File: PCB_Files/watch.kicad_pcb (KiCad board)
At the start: 4 copper layers, 40 x 40 mm, 118 parts, among them J1 Conn_01x13_MountingPin, J3 Conn_01x02_Pin, P1 USB_C_Plug_USB2.0, Q1 BC847, Q2 BC847, Q3 FS8205A, Q4 BSS138, Q5 BSS138, Q8 BC847, SW1 SW_Push, SW2 SW_Push, U1 APS6404L-3SQRx-ZR, U10 LSM6DS3, U11 MAX-M10S, U12 MCP1700x-120xxMB, U13 DRV2605LDGS, U2 ESP32-PICO-D4, U3 CP2102N-Axx-xQFN28, U4 TPS7A0533PDBV, U5 MCP73831-2-OT, U6 AP9101CK6, U7 MAX30105EFD_T, U8 W25Q128JVS, U9 BMP388, Y1 SG-3030CM

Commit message: Added new ZIF connector footprint and made changes in schematics
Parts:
- moved AE1 89.0 mm to (131.4, 82.7)
- moved TP2 79.3 mm to (143.6, 92.6)
- moved TP1 76.5 mm to (145.6, 92.6)
- moved TP3 71.2 mm to (153.8, 93.8)
- moved TP5 71.0 mm to (156.1, 96.9)
- moved TP4 71.0 mm to (154.1, 96.6)
- moved TP6 69.6 mm to (158.5, 96.9)
- moved C31 3.91 mm to (160.7, 99.6), turned to -90 degrees
- moved C19 3.43 mm to (157.2, 90.2)
- moved U4 1.39 mm to (156.6, 93.8), turned to 90 degrees
- moved U2 1.21 mm to (143.5, 97.9)
- moved U12 0.98 mm to (157.4, 100.5)
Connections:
- TP2 pad 1: unconnected-(TP2-Pad1) -> /U0TXD

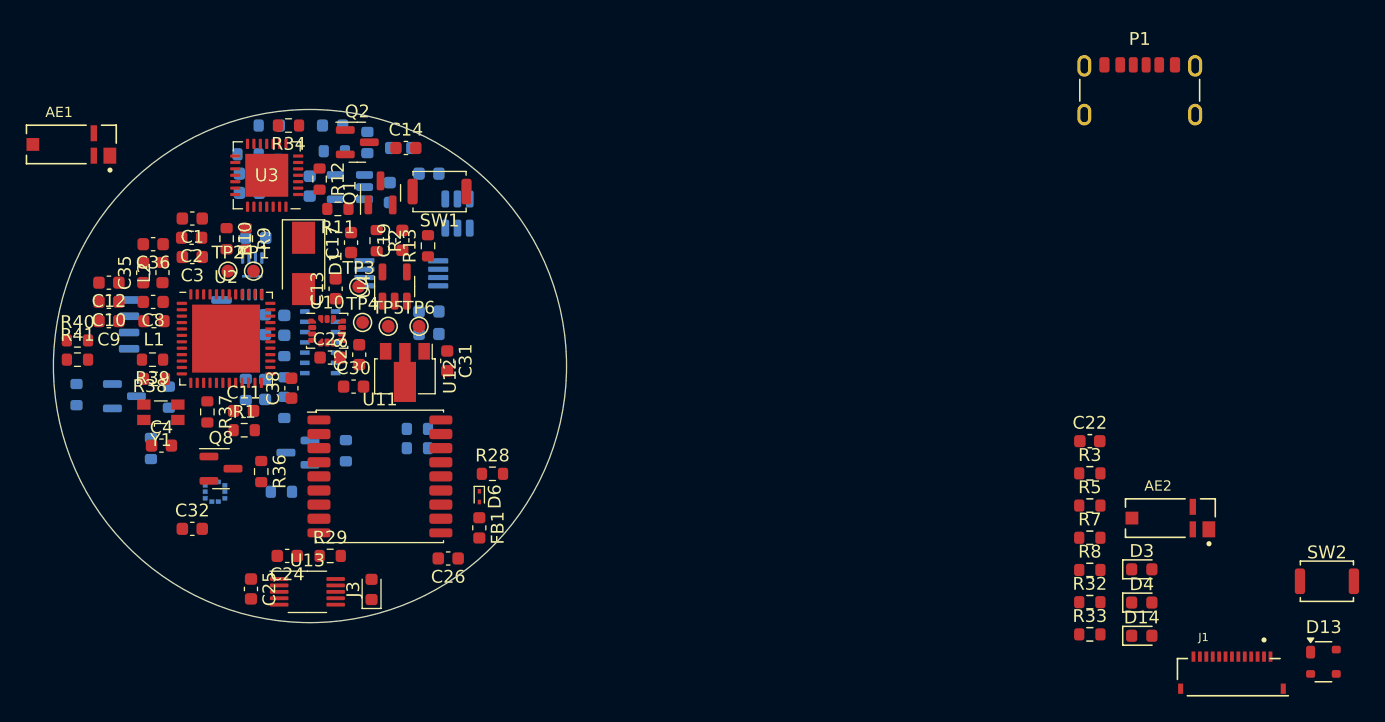
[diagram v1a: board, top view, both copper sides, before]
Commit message: Adding missing footprints and making cAD
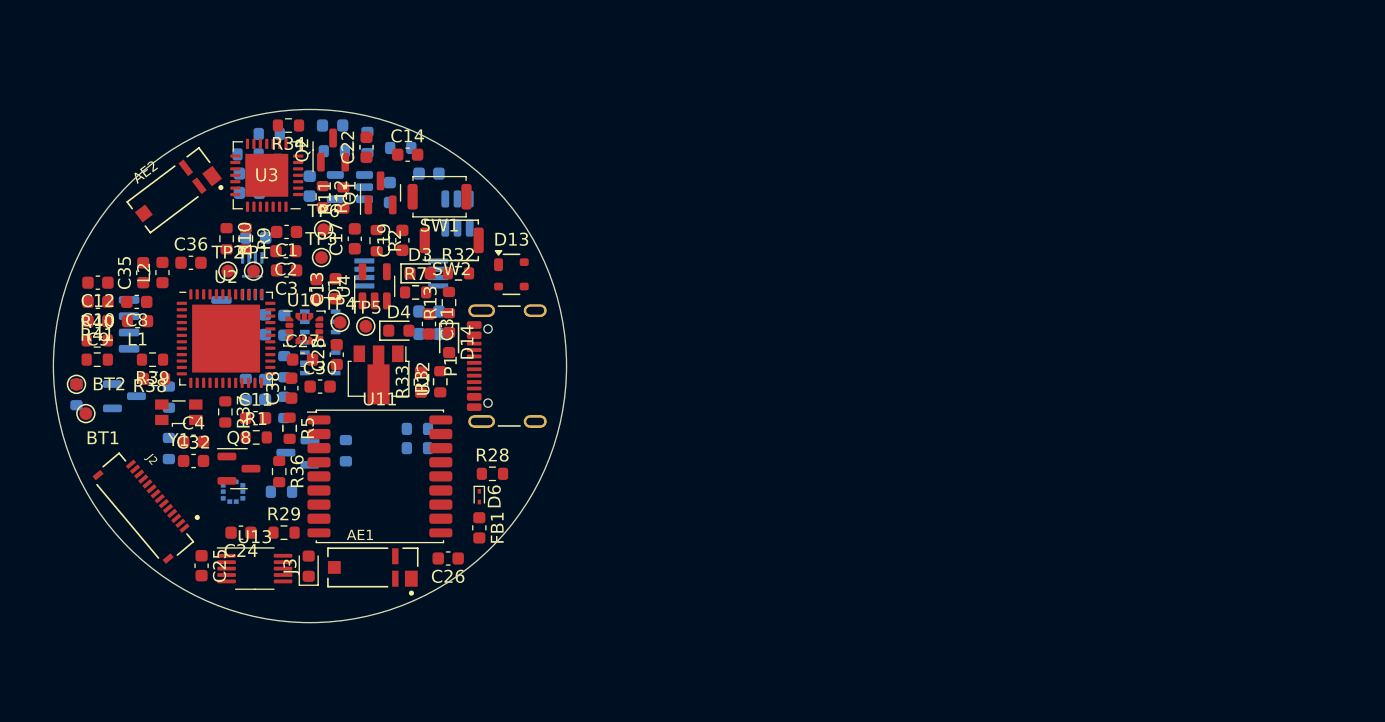
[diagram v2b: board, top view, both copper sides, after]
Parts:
- removed J1: Conn_01x13_MountingPin, footprints:HRS_FH34SRJ-12S-0.5SH_50_
- removed R8: 330, Resistor_SMD:R_0603_1608Metric
- added BT1: BT1, TestPoint:TestPoint_Pad_D1.0mm, F.Cu at (132.5, 103.7)
- added BT2: BT2, TestPoint:TestPoint_Pad_D1.0mm, F.Cu at (131.8, 101.4)
- added J2: Conn_01x14_MountingPin, footprints:HRS_FH34SRJ-14S-0.5SH_50_, F.Cu at (137.2, 111.0)
- D1: footprint Diode_SMD:D_SMA -> Capacitor_SMD:C_0603_1608Metric
- P1: footprint Connector_USB:USB_C_Receptacle_GCT_USB4125-xx-x-0190_6P_TopMnt_Horizontal -> Connector_USB:USB_C_Receptacle_GCT_USB4105-xx-A_16P_TopMnt_Horizontal
- moved AE2 81.7 mm to (139.4, 86.3), turned to 37 degrees
- moved SW2 73.2 mm to (161.1, 90.2), turned to 180 degrees
- moved D13 70.1 mm to (165.7, 92.8)
- moved R5 62.7 mm to (148.4, 104.8), turned to -90 degrees
- moved D4 61.7 mm to (156.9, 97.2)
- moved C22 60.9 mm to (154.4, 82.9), turned to 90 degrees
- moved D3 60.8 mm to (158.6, 92.8)
- moved D14 58.6 mm to (160.8, 98.2), turned to -90 degrees
- moved R7 55.9 mm to (158.2, 94.3)
- moved R33 55.7 mm to (158.7, 101.2), turned to 90 degrees
- moved R32 55.5 mm to (161.6, 92.8)
- moved P1 52.3 mm to (166.5, 100.0), turned to 90 degrees
- moved R3 51.1 mm to (160.2, 101.2), turned to 90 degrees
- moved AE1 40.5 mm to (154.9, 115.7)
- moved TP6 10.6 mm to (151.1, 89.4)
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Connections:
- D4 pad 1: Net-(D4-K) -> GND
- U8 pad 4: unconnected-(U8-GND-Pad4) -> GND

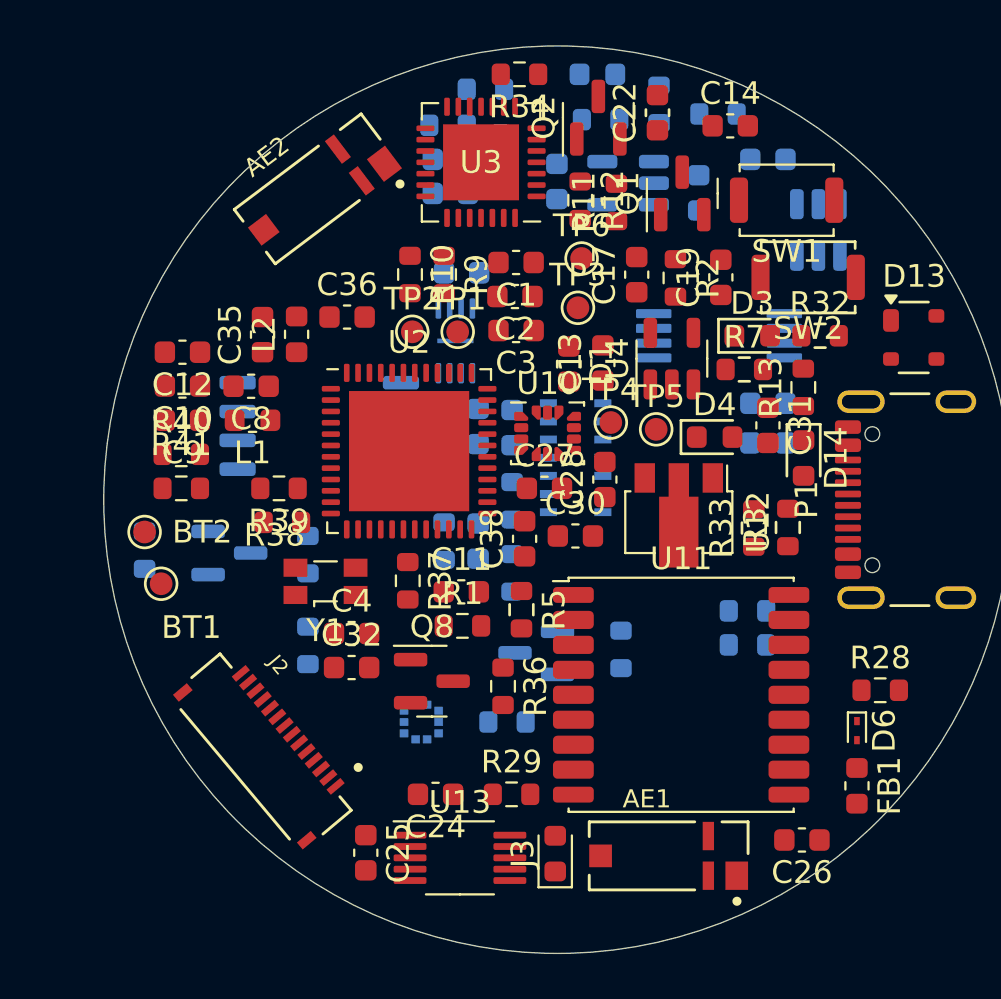
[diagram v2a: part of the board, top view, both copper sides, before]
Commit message: changed place of some components and fixed antenna
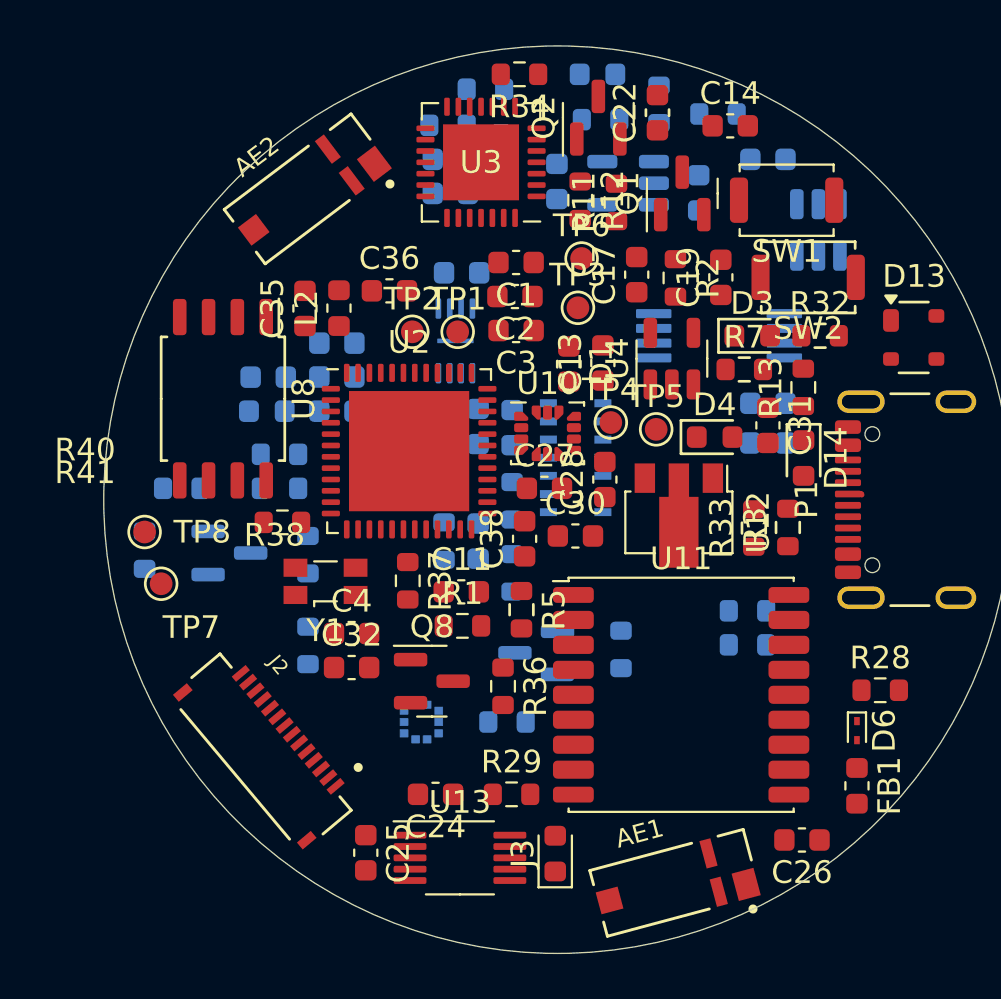
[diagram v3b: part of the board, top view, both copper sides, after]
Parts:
- removed R10, R9: 1k, Resistor_SMD:R_0603_1608Metric
- C10, C12, C8, C9, L1, R39, R40, R41: moved to B.Cu
- TP7: renamed from BT1; value BT1 -> TestPoint
- TP8: renamed from BT2; value BT2 -> TestPoint
- U8: moved to F.Cu
- moved C12 6.82 mm to (140.3, 93.1), turned to 0 degrees
- moved C9 6.82 mm to (140.3, 96.1), turned to 0 degrees
- moved C10 6.82 mm to (140.3, 94.6), turned to 0 degrees
- moved U8 4.41 mm to (135.3, 95.5), turned to -90 degrees
- moved R40 4.33 mm to (137.7, 98.0), turned to 180 degrees
- moved R41 4.33 mm to (137.7, 99.5), turned to 180 degrees
- moved R39 4.29 mm to (133.4, 99.5), turned to 0 degrees
- moved C36 2.20 mm to (142.6, 90.8)
- moved L2 2.20 mm to (140.4, 91.6)
- moved C35 2.20 mm to (138.9, 91.6)
- moved AE1 1.22 mm to (155.2, 116.9), turned to 15 degrees
- moved C8 0.85 mm to (137.2, 94.6), turned to 0 degrees
- moved L1 0.75 mm to (137.2, 96.1), turned to 0 degrees
- moved AE2 0.44 mm to (139.0, 86.3)
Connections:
- AE1 pad 1: Net-(AE1-A) -> (no net)
- AE1 pad 3: (no net) -> Net-(AE1-A)
- AE2 pad 1: Net-(AE2-A) -> (no net)
- AE2 pad 3: (no net) -> Net-(AE2-A)
- D13 pad 2: Net-(P1-D+) -> /D+
- D13 pad 3: Net-(P1-D-) -> /D-
- P1 pad A6: Net-(P1-D+) -> /D+
- P1 pad A7: Net-(P1-D-) -> /D-
- U3 pad 25: Net-(U3-RXD) -> /U0TXD
- U3 pad 26: Net-(U3-TXD) -> /U0RXD
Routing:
- net /D-: track 0.00 -> 0.62 mm

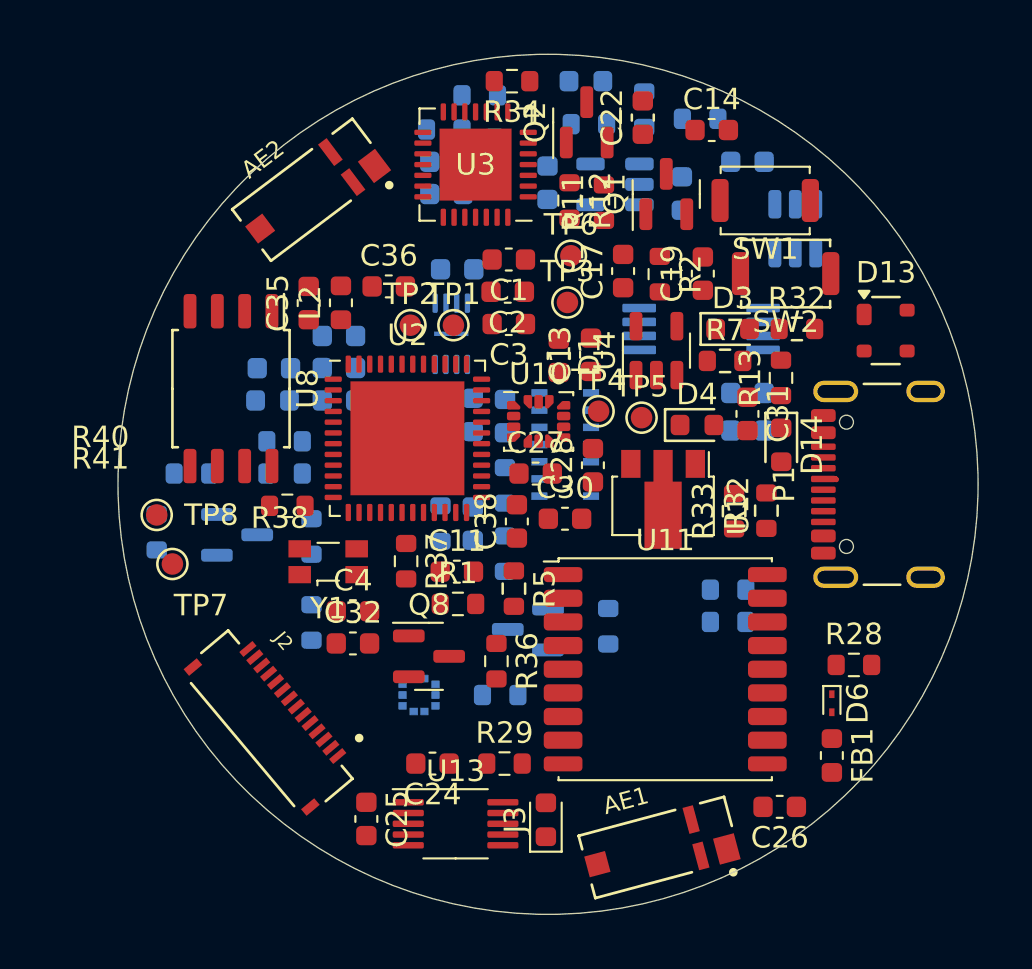
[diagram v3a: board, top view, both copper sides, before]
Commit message: Making major changes in the schematic, added a external 40MHz crystal oscilator and did routing
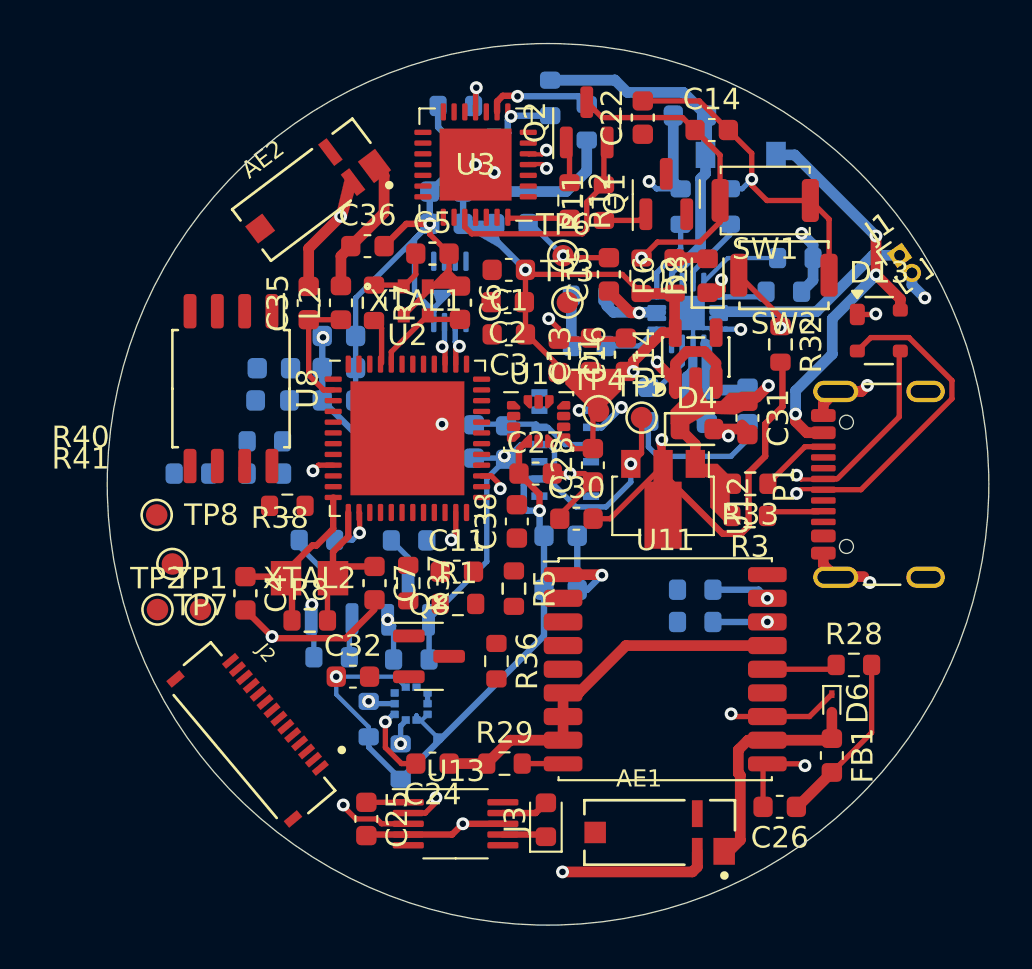
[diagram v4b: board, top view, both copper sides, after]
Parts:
- removed C20: 10 uF, Capacitor_SMD:C_0603_1608Metric
- removed D14: D_Zener, Diode_SMD:D_0603_1608Metric
- removed D3, D5: LED, LED_SMD:LED_0603_1608Metric
- removed Q3: FS8205A, footprints:SOP65P640X120-8N
- removed R13: 2.7k, Resistor_SMD:R_0603_1608Metric
- removed R14, R15: 330, Resistor_SMD:R_0603_1608Metric
- removed R16: 2k, Resistor_SMD:R_0603_1608Metric
- removed R17, R30: 0R, Resistor_SMD:R_0603_1608Metric
- removed U4: TPS7A0533PDBV, Package_TO_SOT_SMD:SOT-23-5
- removed U5: MCP73831-2-OT, Package_TO_SOT_SMD:SOT-23-5
- removed U6: AP9101CK6, Package_TO_SOT_SMD:SOT-23-6
- removed Y1: SG-3030CM, Oscillator:Oscillator_SMD_SeikoEpson_SG3030CM
- added C23: 1uF, Capacitor_SMD:C_0603_1608Metric, B.Cu at (156.6, 82.8)
- added C33: 4.7uF, Capacitor_SMD:C_0603_1608Metric, B.Cu at (157.4, 96.4)
- added D2: LED, LED_SMD:LED_0603_1608Metric, B.Cu at (154.7, 96.3)
- added D7: LED, LED_SMD:LED_0603_1608Metric, B.Cu at (151.9, 93.6)
- added D8: LED, LED_SMD:LED_0603_1608Metric, F.Cu at (157.4, 90.3)
- added D9: SS14FL, footprints:SOD-123FL, B.Cu at (159.0, 84.7)
- added J1: Conn_01x02_Pin, Connector_PinHeader_1.00mm:PinHeader_1x02_P1.00mm_Vertical, F.Cu at (166.3, 89.3)
- added R10: 1.18k, Resistor_SMD:R_0603_1608Metric, B.Cu at (156.2, 87.1)
- added R24: 1.13k, Resistor_SMD:R_0603_1608Metric, B.Cu at (161.5, 89.5)
- added R25: 1.5k, Resistor_SMD:R_0603_1608Metric, B.Cu at (151.9, 91.2)
- added R42: 1.5k, Resistor_SMD:R_0603_1608Metric, B.Cu at (159.3, 96.3)
- added R43: 10k, Resistor_SMD:R_0603_1608Metric, B.Cu at (161.0, 91.0)
- added R6: 0.3k, Resistor_SMD:R_0603_1608Metric, F.Cu at (155.9, 90.3)
- added R8: 0R, Resistor_SMD:R_0603_1608Metric, F.Cu at (138.9, 106.3)
- added R9: 4.12k, Resistor_SMD:R_0603_1608Metric, B.Cu at (158.5, 87.1)
- added U14: TLV75533PDBV, Package_TO_SOT_SMD:SOT-23-5, F.Cu at (156.9, 94.1)
- added U15: BQ24074RGT, Package_DFN_QFN:VQFN-16-1EP_3x3mm_P0.5mm_EP1.6x1.6mm, B.Cu at (156.5, 92.0)
- added XTAL1: ECS-400-10-37B2-CKY-TR, footprints:ECX-1637B2_ECS, F.Cu at (143.8, 91.5)
- added XTAL2: FC-135R 32.7680KA-A3, footprints:XTAL_KA-A3_EPS, F.Cu at (138.9, 104.4)
- C15, C16: value 100nF -> 22uF; moved to F.Cu
- C17: value 1 uF -> 0.1 uF; moved to B.Cu
- C19, R34: moved to B.Cu
- C4: value 0.1 uF -> 12.5pF
- C5: value 0.1 uF -> 8pF; moved to F.Cu
- C6: value 4.7 uF -> 10pF; moved to F.Cu
- C7: value 4.7 uF -> 12.5pF; moved to F.Cu
- R7: value 330 -> 10k
- moved C7 23.1 mm to (141.9, 104.6), turned to -90 degrees
- moved TP1 17.7 mm to (133.8, 105.8)
- moved TP2 17.7 mm to (131.8, 105.8)
- moved R7 16.5 mm to (141.9, 91.6), turned to -90 degrees
- moved C19 16.1 mm to (150.6, 104.9), turned to 180 degrees
- moved C5 15.3 mm to (144.6, 89.3), turned to 0 degrees
- moved C17 12.7 mm to (150.6, 102.4), turned to 180 degrees
- moved R19 10.00 mm to (139.9, 108.0), turned to 0 degrees
- moved C15 9.71 mm to (152.8, 90.2), turned to 90 degrees
- moved R20 9.29 mm to (143.6, 108.1), turned to 180 degrees
- moved C6 6.91 mm to (145.9, 91.6), turned to -90 degrees
- moved R4 6.63 mm to (151.8, 83.2), turned to 90 degrees
- moved C16 5.93 mm to (153.6, 94.0), turned to 90 degrees
- moved Q4 5.74 mm to (143.5, 105.4), turned to 90 degrees
- moved R22 5.57 mm to (143.1, 112.9), turned to 90 degrees
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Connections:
- C15 pad 1: /VBUS -> /Batt+
- C16 pad 1: /VBUS -> /3V3
- C17 pad 1: /Batt+ -> GND
- C17 pad 2: GND -> /3V3
- C19 pad 1: /3V3 -> GND
- C19 pad 2: GND -> /3V3
- C4 pad 1: /3V3 -> /32K_P
- C5 pad 1: /C5 -> Net-(XTAL1-IN/OUT)
- C6 pad 1: /VBUS -> GND
- C6 pad 2: GND -> /XTAL_N
- C7 pad 1: /Batt+ -> /32K_N
- J2 pad 13: /CTP_RST -> /EN
- J2 pad 8: /RST -> /EN
- R34 pad 1: /VBUS -> /EXT_5V
- R7 pad 1: Net-(D3-K) -> Net-(XTAL1-IN/OUT)
- R7 pad 2: GND -> /XTAL_P
- U2 pad 12: /32K_XP -> /32K_P
- U2 pad 13: /RS -> /32K_N
- U2 pad 15: /RST -> unconnected-(U2-IO26-Pad15)
- U2 pad 17: /CTP_RST -> /RS
- U2 pad 44: unconnected-(U2-XTAL_N_NC-Pad44) -> /XTAL_N
- U2 pad 45: unconnected-(U2-XTAL_P_NC-Pad45) -> /XTAL_P
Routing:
- net GND: track 0.00 -> 143.4 mm, vias 0 -> 25
- net /3V3: track 0.00 -> 133.3 mm, vias 0 -> 6
- net /D+: track 0.00 -> 44.2 mm, vias 0 -> 2
- net /1.8V: track 0.00 -> 39.0 mm, vias 0 -> 3
- net /D-: track 0.62 -> 37.7 mm, vias 0 -> 2
- net /EN: track 0.00 -> 35.1 mm, vias 0 -> 2
- net /GPIO0: track 0.00 -> 26.2 mm, vias 0 -> 2
- net /LV_SDA: track 0.00 -> 25.3 mm, vias 0 -> 2
- net /SCL_i2c: track 0.00 -> 22.1 mm, vias 0 -> 3
- net /SDA: track 0.00 -> 20.3 mm, vias 0 -> 3
- net /VBUS: track 0.00 -> 20.1 mm, vias 0 -> 3
- net /Batt+: track 0.00 -> 17.8 mm, vias 0 -> 2
- net /LV_SCL: track 0.00 -> 16.7 mm, vias 0 -> 2
- net /EXT_5V: track 0.00 -> 15.0 mm
- net Net-(AE1-A): track 0.00 -> 11.0 mm
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- removed copper zone on In2.Cu, net /3V3
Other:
- board size 40 x 40 mm -> 41 x 41 mm
